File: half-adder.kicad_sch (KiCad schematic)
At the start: 55 parts, among them J1 A, J2 B, J3 C, J4 OUTPUT, J5 CARRY OUT, J6 5V, J7 GROUND, Q13 BC547, Q15 BC547, Q2 BC547, Q20 BC547, Q24 BC547, Q7 BC547

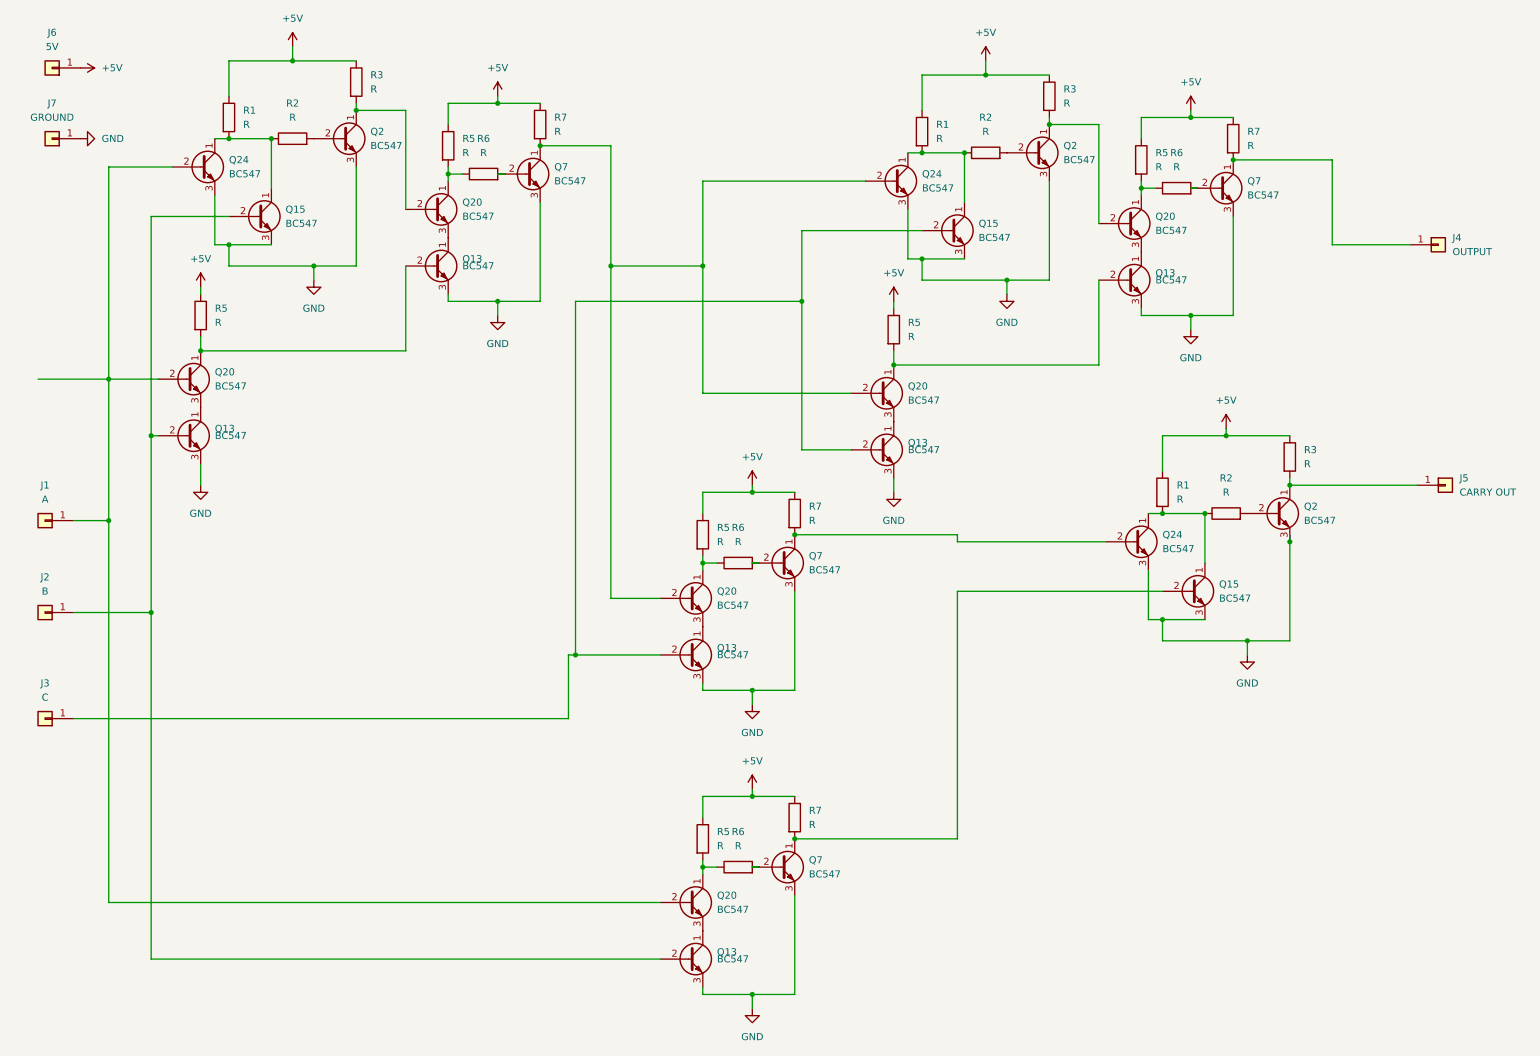
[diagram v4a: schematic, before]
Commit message: Ngspice simulation
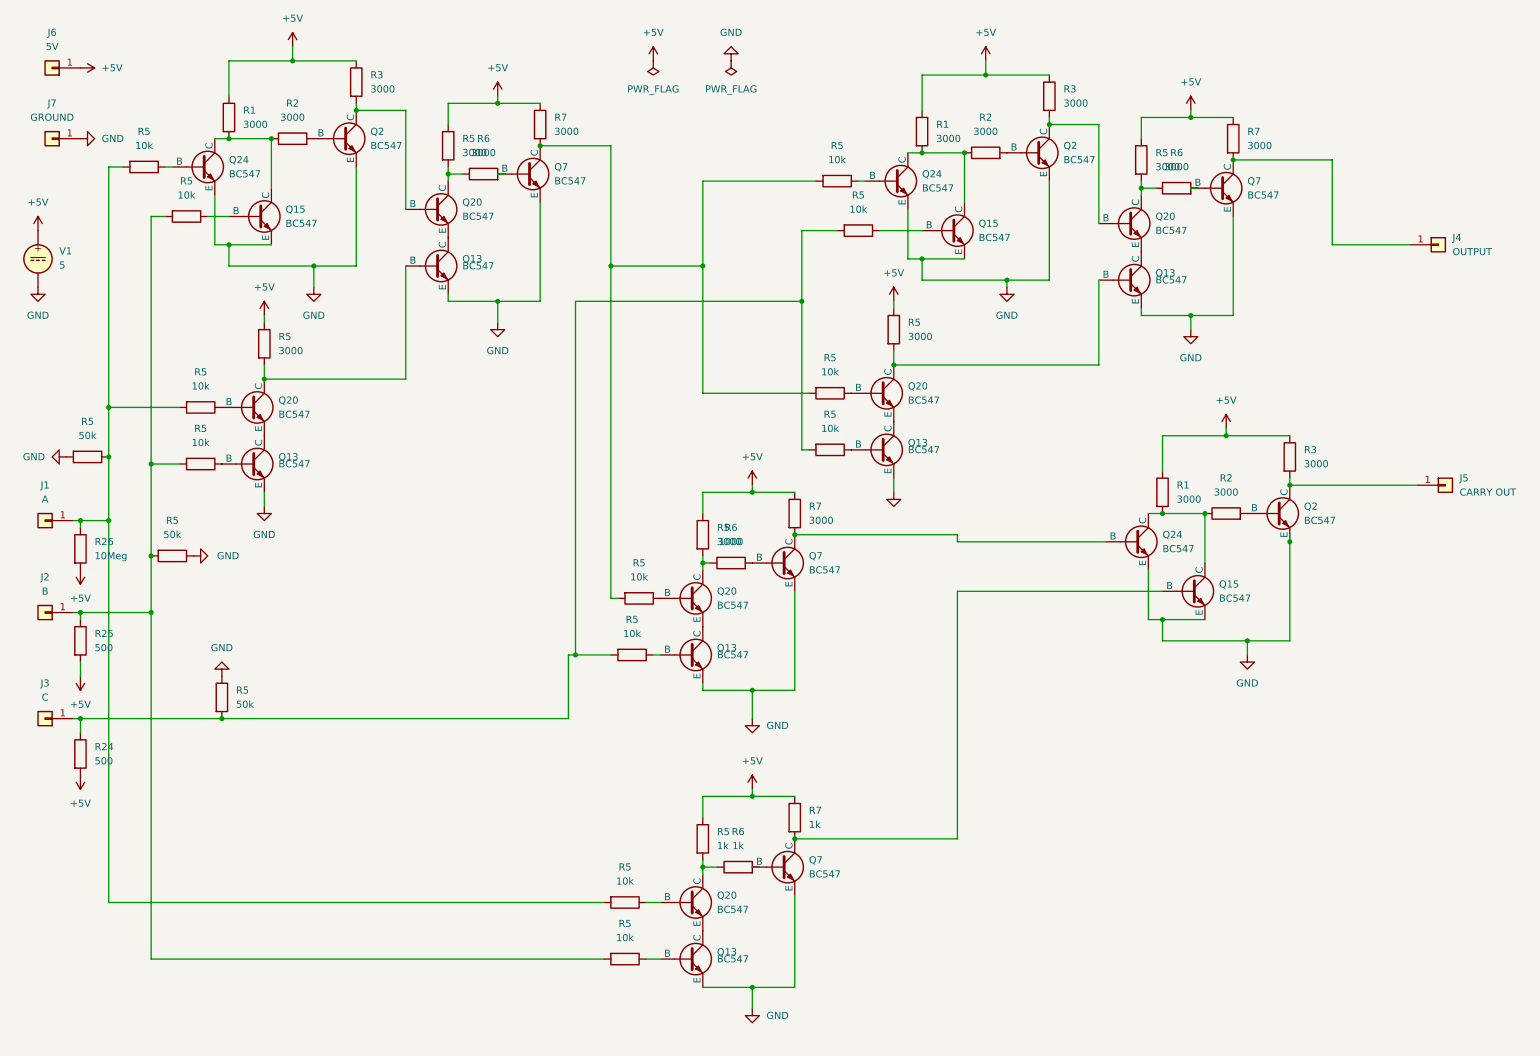
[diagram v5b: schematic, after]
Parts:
- added R24, R25: 500, symbol Device:R
- added R26: 10Meg, symbol Device:R
- added R5 (x12): 10k, Resistor_THT:R_Axial_DIN0207_L6.3mm_D2.5mm_P10.16mm_Horizontal, symbol Device:R
- added R5 (x3): 50k, Resistor_THT:R_Axial_DIN0207_L6.3mm_D2.5mm_P10.16mm_Horizontal, symbol Device:R
- added V1: 5, symbol Simulation_SPICE:VDC
- Q13, Q15, Q2, Q20, Q24, Q7: symbol Transistor_BJT:BC547 -> Simulation_SPICE:NPN
- R1, R2, R3, R5, R6, R7: value R -> 3000
- R5, R6, R7: value R -> 1k
- R6: value R -> 1000
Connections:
- net +5V: now also R24.2, R25.2, R26.2, V1.1
- net GND: now also R5.1, R5.1, R5.2, V1.2
- new net: Q20.2 (B), R5.1 (x4)
- new net: Q7.1 (C), R5.2, R5.2, R5.2, R7.2
- new net: Q24.2 (B), R5.1 (x2)
- new net: Q15.2 (B), R5.1 (x2)
- new net: J2.1 (Pin_1), R25.1, R5.2, R5.2, R5.2, R5.2
- new net: J1.1 (Pin_1), R26.1, R5.1, R5.2, R5.2, R5.2
- new net: Q13.2 (B), R5.1 (x4)
- new net: J3.1 (Pin_1), R24.1, R5.2, R5.2, R5.2, R5.2
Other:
- moved on the sheet: R5, R6

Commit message: Add ground plane to half adder and modularize or gate
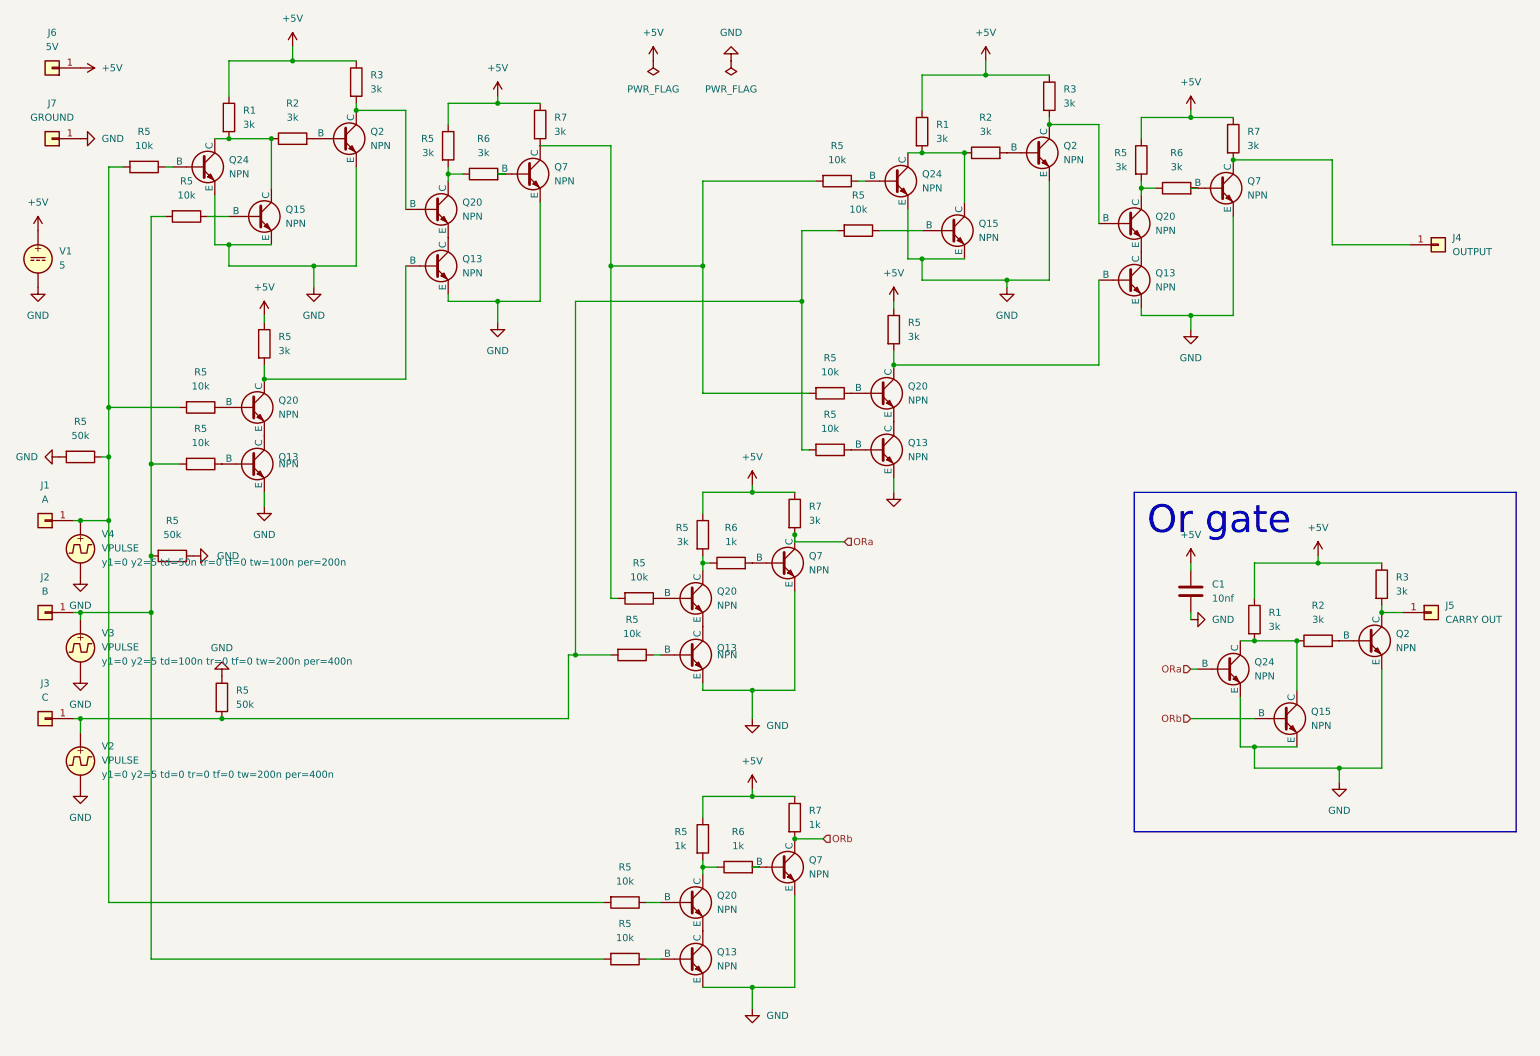
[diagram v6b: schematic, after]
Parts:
- removed R24, R25: 500, symbol Device:R
- removed R26: 10Meg, symbol Device:R
- added C1: 10nf, symbol Device:C
- added V2, V3, V4: VPULSE, symbol Simulation_SPICE:VPULSE
- Q13, Q15, Q2, Q20, Q24, Q7: value BC547 -> NPN; footprint Package_TO_SOT_THT:TO-92_Inline -> SOT-23-3_L2.9-W1.6-P1.90-LS2.8-BR:SOT-23-3_L2.9-W1.6-P1.90-LS2.8-BR; JLC_3DModel_Q (none) -> 62a57c6760504a01965db6419a6d07df; JLC_3D_Size (none) -> 2.5 2.9; LCSC (none) -> C239009
- R1, R2, R3, R5, R6, R7: value 3000 -> 3k; footprint Resistor_THT:R_Axial_DIN0207_L6.3mm_D2.5mm_P10.16mm_Horizontal -> R0603:R0603; LCSC (none) -> C4211
- R5, R6, R7: footprint Resistor_THT:R_Axial_DIN0207_L6.3mm_D2.5mm_P10.16mm_Horizontal -> R0603:R0603; LCSC (none) -> C4211
- R6: value 1000 -> 1k; footprint Resistor_THT:R_Axial_DIN0207_L6.3mm_D2.5mm_P10.16mm_Horizontal -> R0603:R0603; LCSC (none) -> C4211
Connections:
- net +5V: now also C1.1
- net GND: now also C1.2, V2.2, V3.2, V4.2
- net ORb: now reaches Q15.2 (B), Q7.1 (C), R7.2
- net at J2.1 (Pin_1), R5.2, R5.2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: now also V3.1
- net at J1.1 (Pin_1), R5.1, R5.2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: now also V4.1
- net at J3.1 (Pin_1), R5.2, R5.2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: now also V2.1
- net ORa: now reaches Q24.2 (B), Q7.1 (C), R7.2
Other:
- note added: "Or gate"
- moved on the sheet: J5, Q15, Q2, Q24, R1, R2, R3, R5

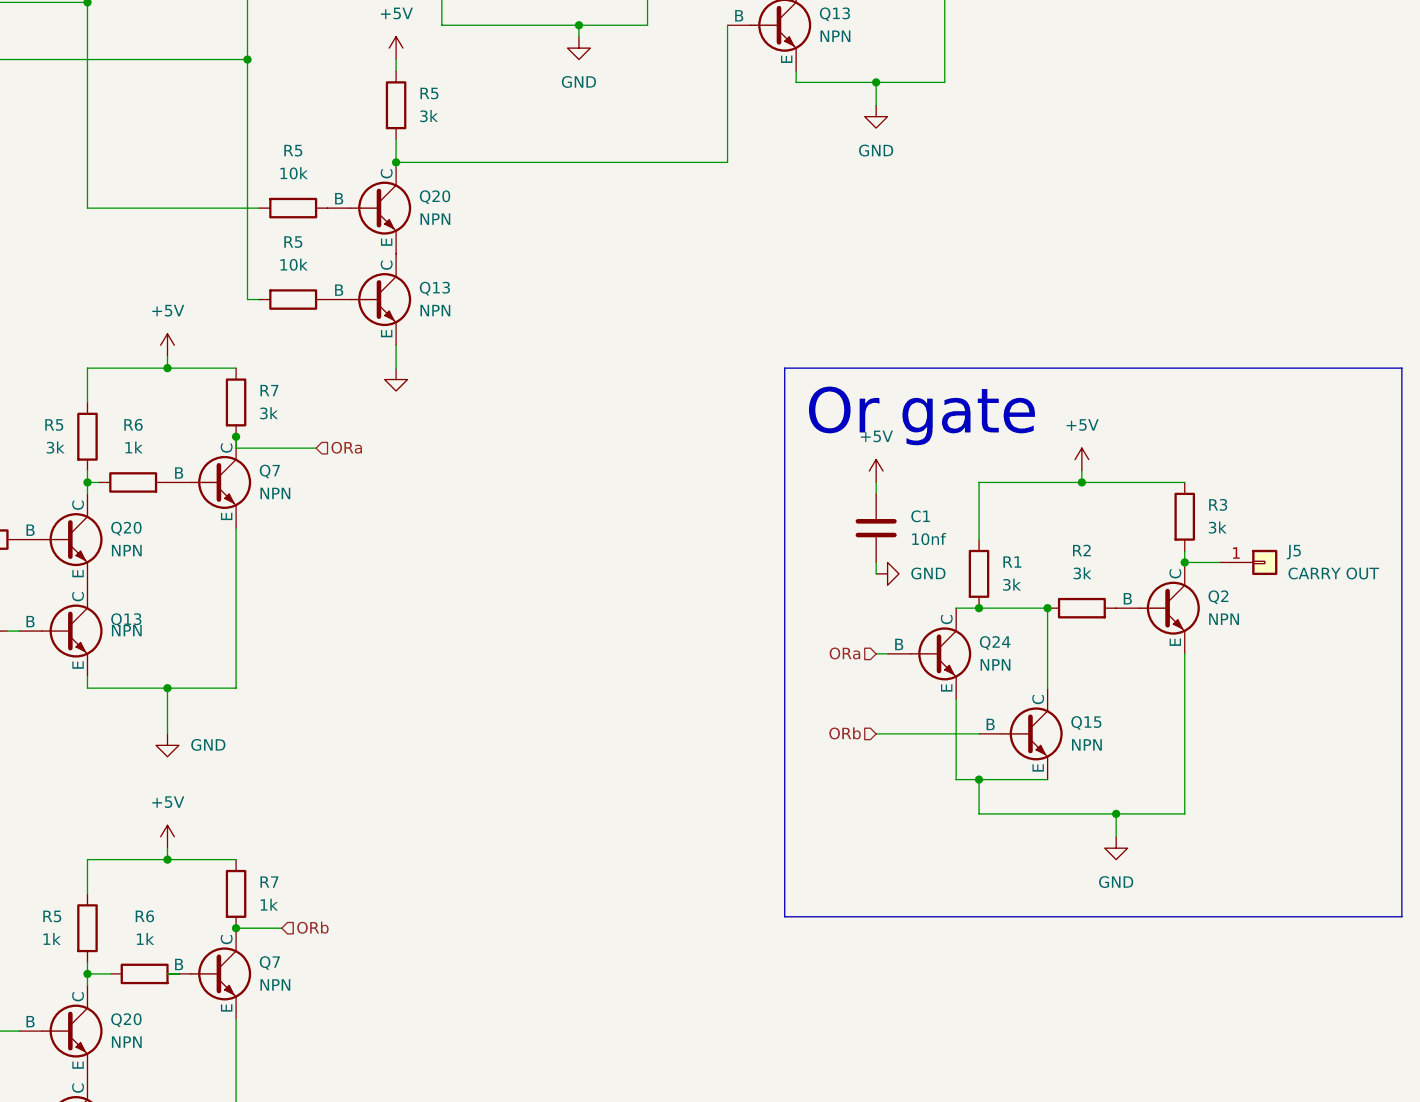
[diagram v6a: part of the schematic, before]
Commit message: Use reusable or gate in half adder
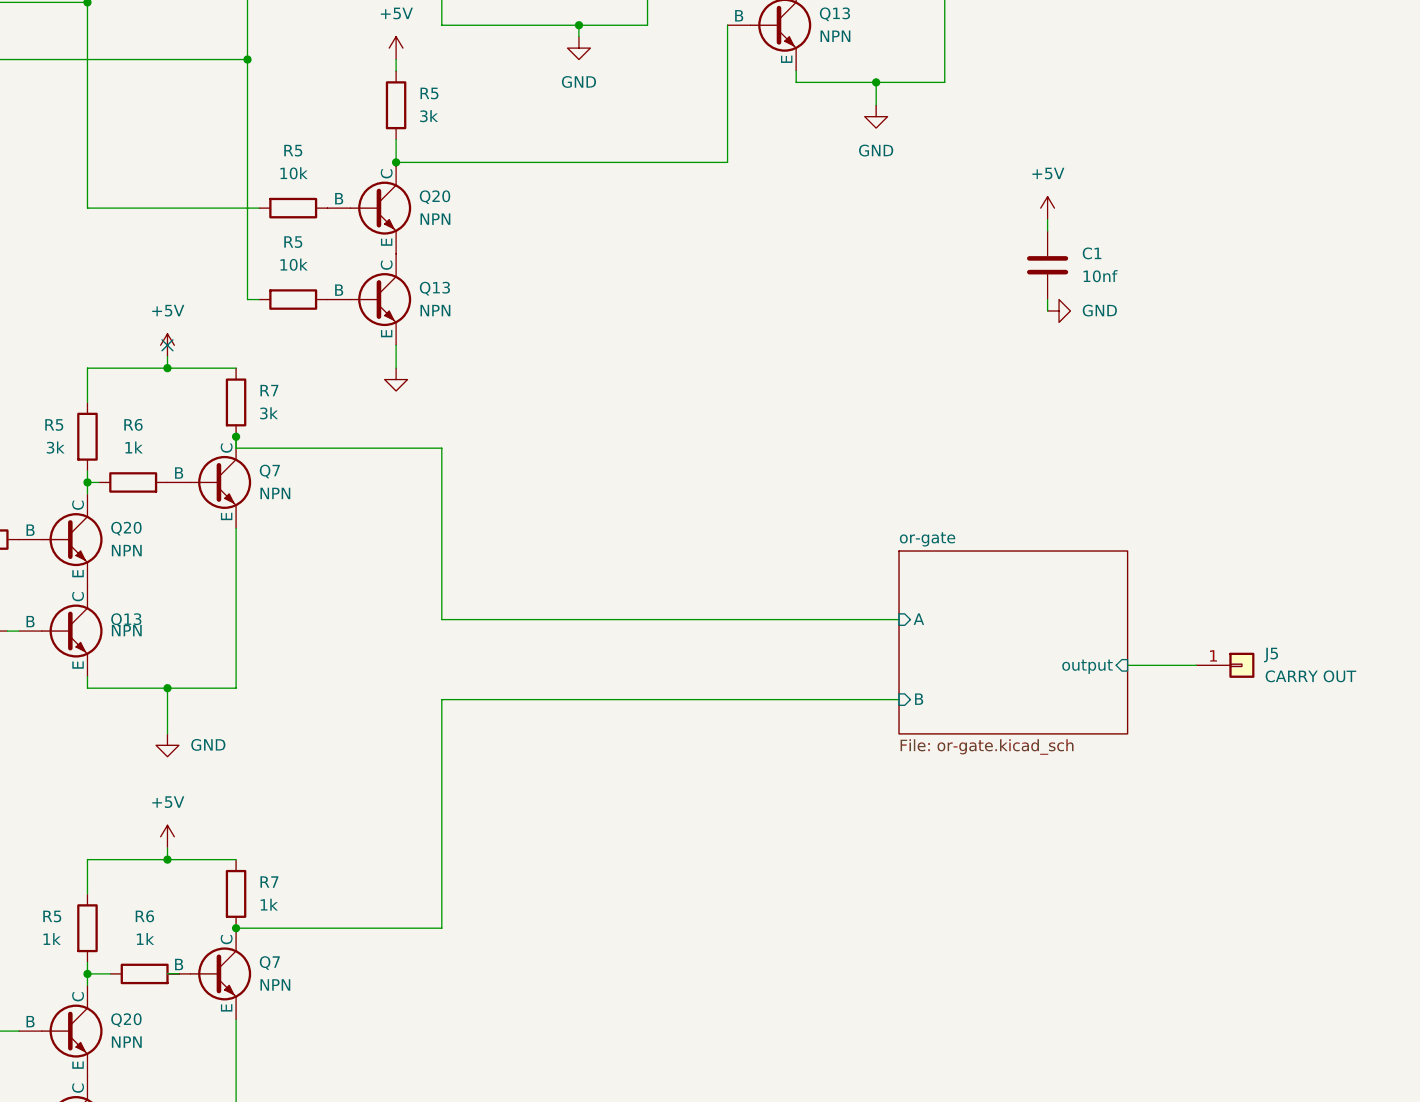
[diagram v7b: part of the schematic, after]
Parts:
- removed Q15, Q2, Q24: NPN, SOT-23-3_L2.9-W1.6-P1.90-LS2.8-BR:SOT-23-3_L2.9-W1.6-P1.90-LS2.8-BR, symbol Simulation_SPICE:NPN
- removed R1, R2, R3: 3k, R0603:R0603, symbol Device:R
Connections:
- net or-gate/output: now reaches J5.1 (Pin_1)
- net ORa renamed or-gate/A
- net ORb renamed or-gate/B
- no-connect marks 0 -> 1
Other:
- added sheet or-gate (or-gate.kicad_sch)
- note removed: "Or gate"
- moved on the sheet: C1
